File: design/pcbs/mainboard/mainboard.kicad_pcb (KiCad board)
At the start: 4 copper layers, 150 x 130 mm, 253 parts, among them J1 Conn_01x01, J10 AudioJackSw, J2 Conn_01x01, J3 Conn_01x01, J4 Conn_01x01, J5 Conn_01x04, J6 Conn_01x04, J7 Conn_Coaxial, J8 Conn_Coaxial, J9 Conn_01x03, K1 EC2-5NU, K2 EC2-5NU, K3 EC2-12NU, K4 EC2-12NU, Q1 SS8050, Q10 SS8550, Q11 SS8050, Q12 SS8050, Q2 SS8050, Q3 SS8550, Q4 SS8050, Q5 SS8050, Q6 SS8050, Q7 SS8050, Q8 SS8050, Q9 SS8050, U1 STM8S003F3P, U10 TPS79318-EP, U11 SRC4392, U12 PCM1792A, U13 OPA1612AxD, U14 Si8645BA-B-IU, U15 OPA1612AxD, U16 TPS7A30, U17 LME49600, U18 OPA1612AxD, U19 TPS7A49, U2 TPS7A49, U20 LME49600, U3 TPS7A30, U4 TLV1117-33, U5 TPS7A49, U6 KC3225K24.5760C1GE00, U7 Combo384, U8 5PB1102, U9 OPA1612AxD

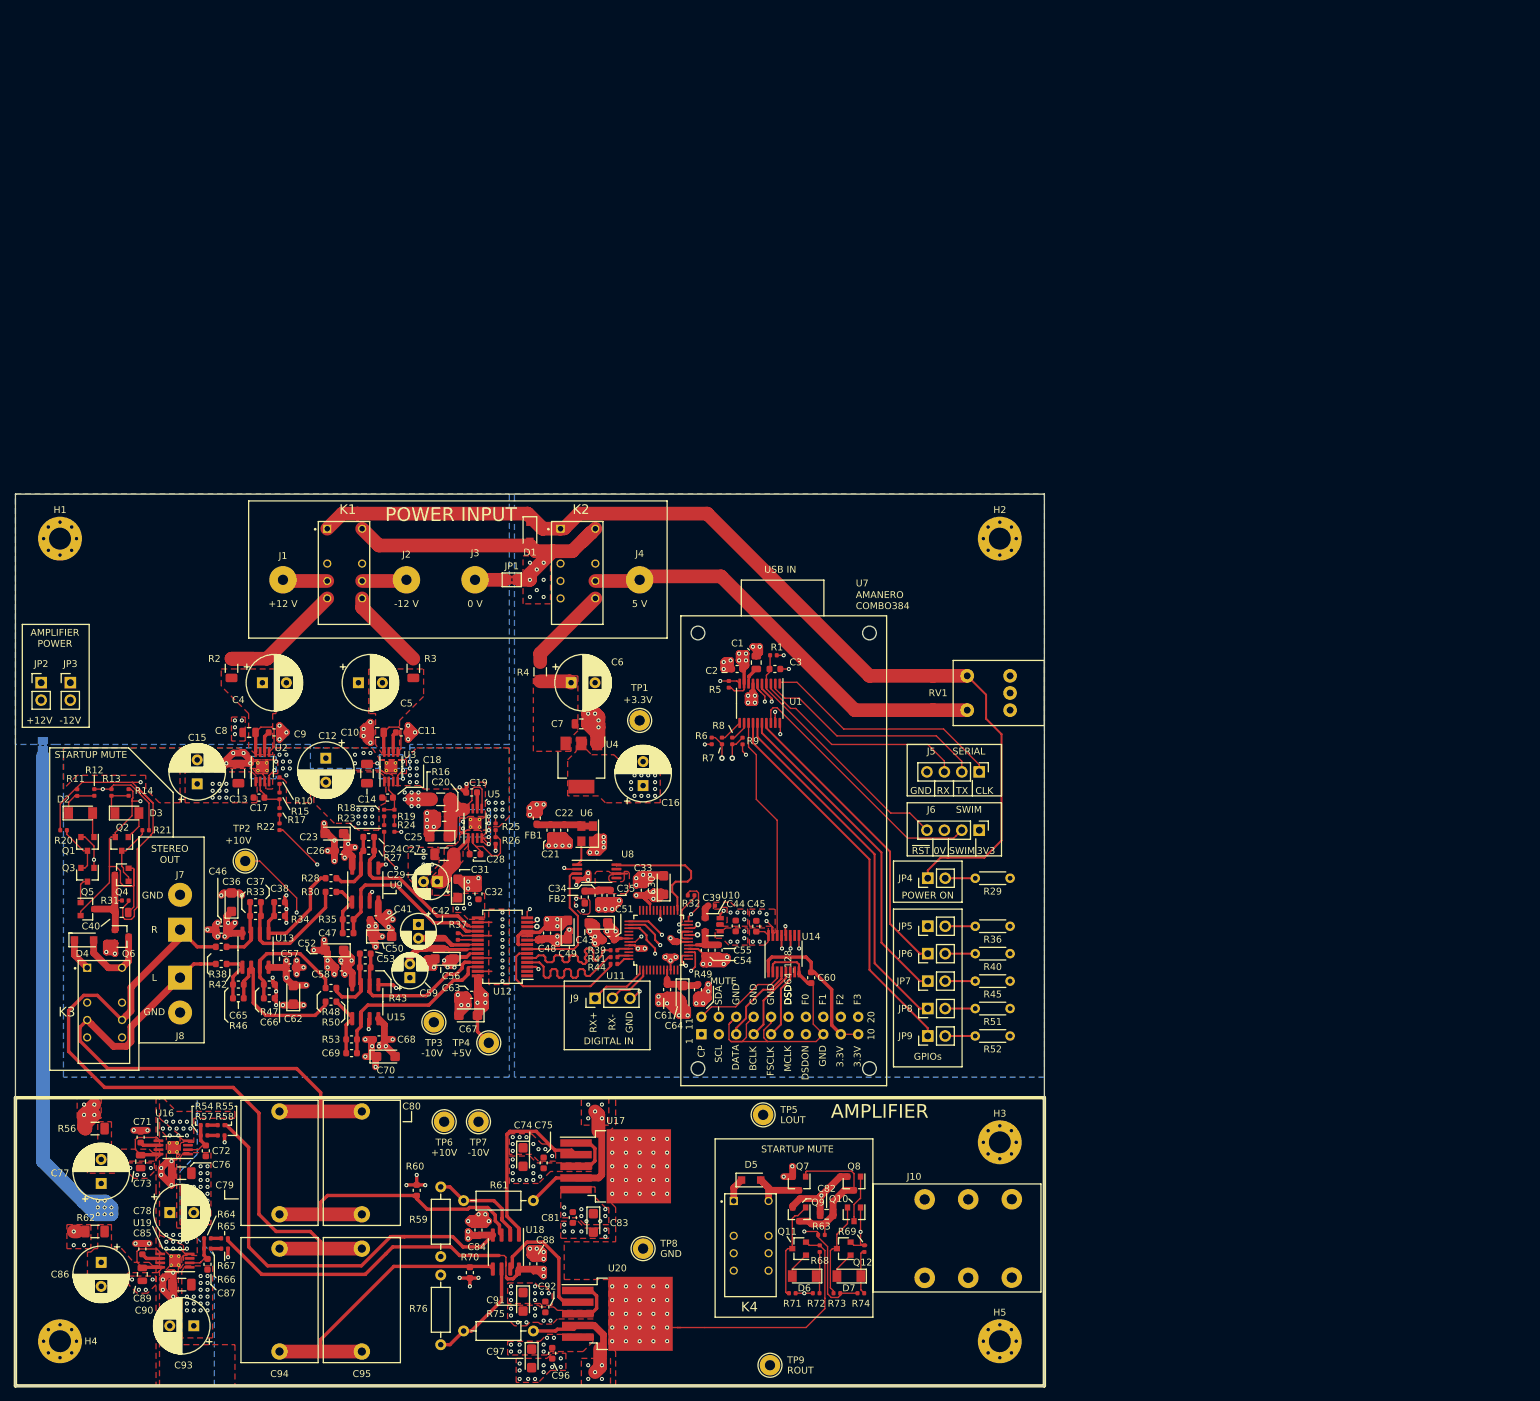
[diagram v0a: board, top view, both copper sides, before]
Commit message: Updated PCB sheet info. Clarified licence in readme.
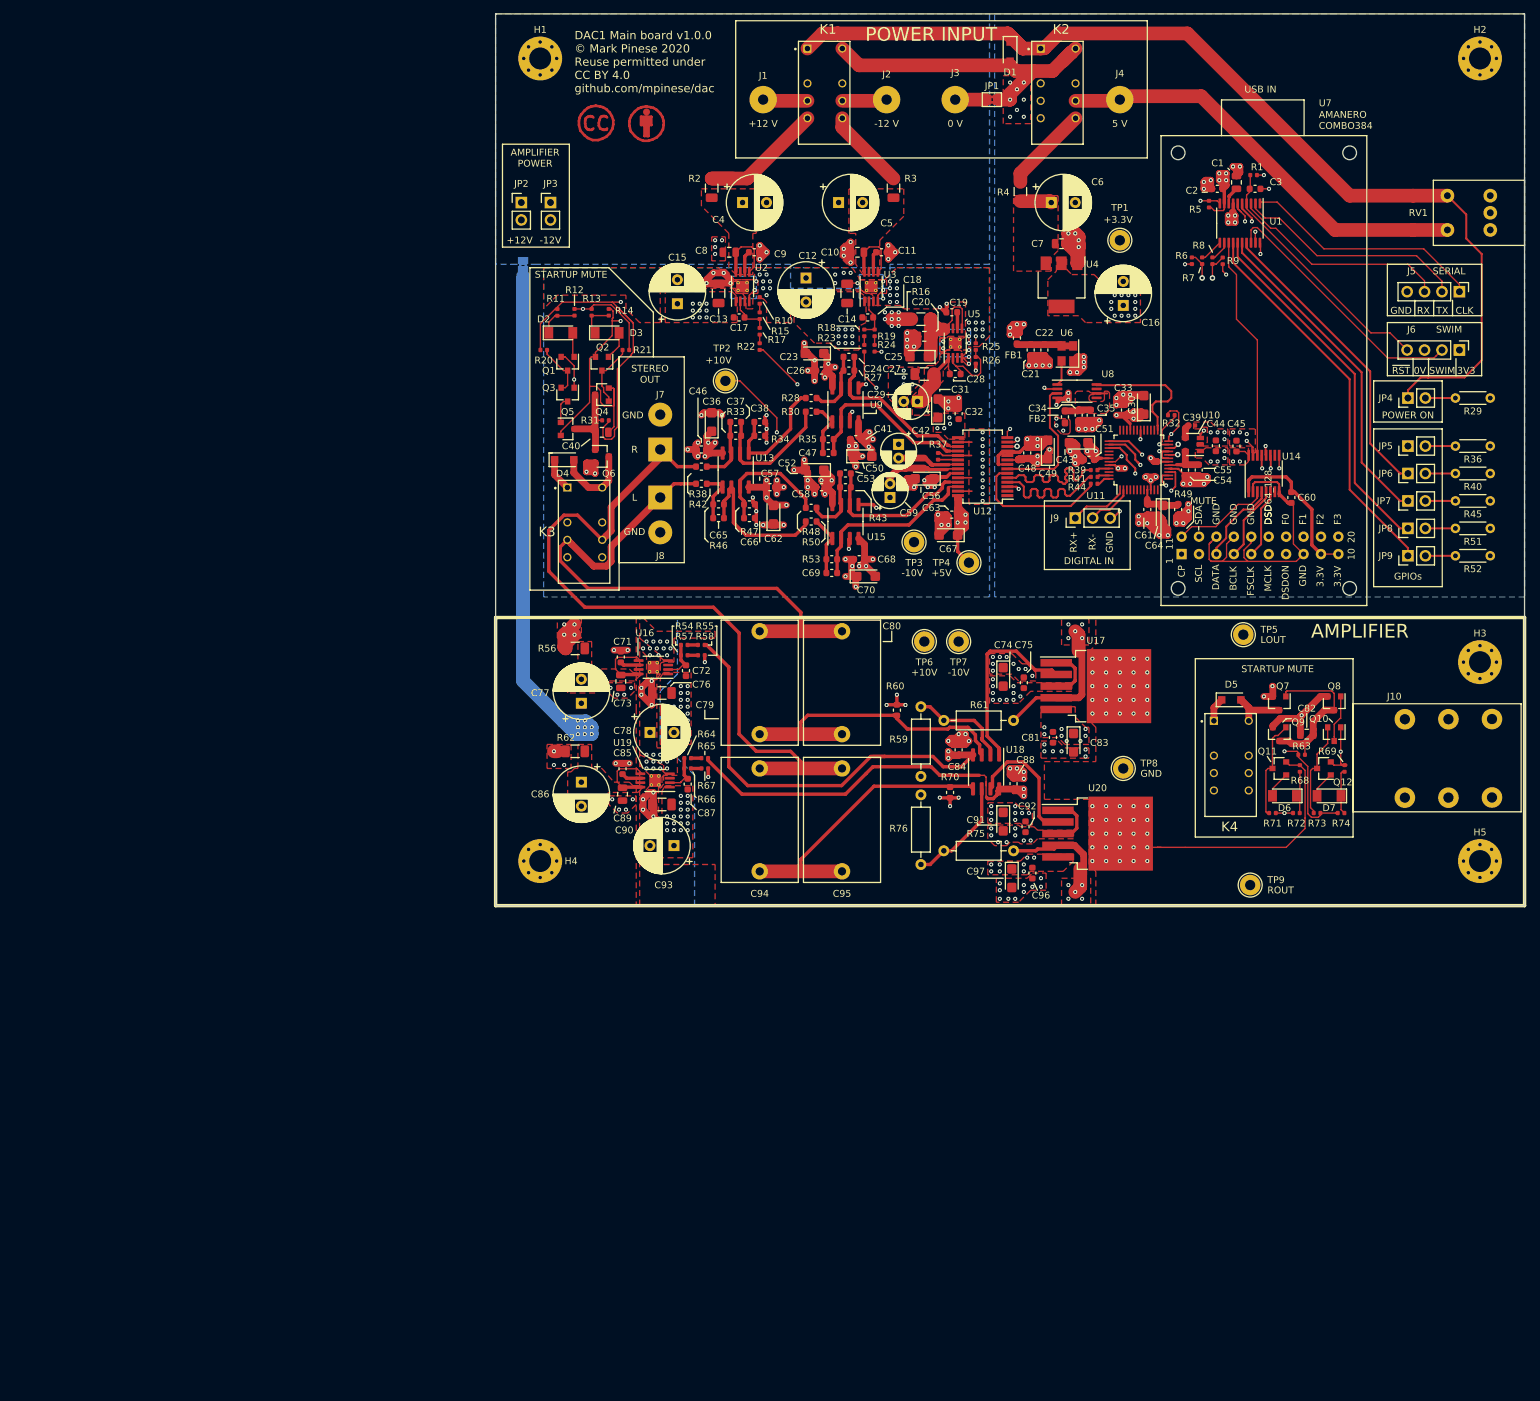
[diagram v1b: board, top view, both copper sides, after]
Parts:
- added REF**: Symbol_CC-Attribution_CopperTop_Small, Symbol:Symbol_CC-Attribution_CopperTop_Small, F.Cu at (82.0, 46.0)
- added REF**: Symbol_CreativeCommons_CopperTop_Type2_Small, Symbol:Symbol_CreativeCommons_CopperTop_Type2_Small, F.Cu at (74.5, 46.0)
- moved U10 99.0 mm to (161.6, 92.8)
- moved R6 99.0 mm to (161.5, 66.0)
- moved R7 99.0 mm to (163.0, 66.0)
- moved R72 99.0 mm to (176.7, 146.5)
- moved R8 99.0 mm to (164.5, 66.0)
- moved C1 99.0 mm to (168.0, 54.6)
- moved C10 99.0 mm to (112.8, 64.8)
- moved C11 99.0 mm to (116.2, 64.8)
- moved C12 99.0 mm to (105.2, 68.5)
- moved C13 99.0 mm to (92.5, 70.8)
- moved C14 99.0 mm to (111.2, 70.8)
- moved C15 99.0 mm to (86.5, 72.2)
- moved C16 99.0 mm to (151.5, 72.5)
- moved C17 99.0 mm to (95.5, 74.2)
- moved C18 99.0 mm to (114.2, 74.2)
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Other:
- board text added: "DAC1 Main board v1.0.0 © Mark Pinese 2020 Reuse permitted under CC BY 4.0 github.com/mpinese/dac"

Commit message: Misc updates
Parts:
- removed REF**: Symbol_CC-Attribution_CopperTop_Small, Symbol:Symbol_CC-Attribution_CopperTop_Small
- removed REF**: Symbol_CreativeCommons_CopperTop_Type2_Small, Symbol:Symbol_CreativeCommons_CopperTop_Type2_Small
- added FB3: Ferrite_Bead_Small, Resistor_SMD:R_0603_1608Metric_Pad1.05x0.95mm_HandSolder, F.Cu at (231.1, 72.5)
- C42, C59: footprint Capacitor_THT:CP_Radial_D5.0mm_P2.00mm -> Capacitor_THT:CP_Radial_D6.3mm_P2.50mm
- R29, R36, R40, R45, R51, R52: value ~ -> Optional
- R39, R41, R44: value 50 -> 10
- R6, R9: value 2.7k -> 2.4k
- moved TP3 113.4 mm to (231.0, 134.8)
- moved TP4 95.0 mm to (224.0, 113.0)
- moved C29 4.37 mm to (119.2, 82.8), turned to 270 degrees
- moved C31 4.01 mm to (128.5, 87.2), turned to 0 degrees
- moved FB1 3.25 mm to (139.0, 76.0), turned to 180 degrees
- moved C67 2.80 mm to (128.5, 104.8), turned to 0 degrees
- moved C56 2.46 mm to (124.8, 98.8), turned to 270 degrees
- moved C59 2.30 mm to (119.8, 101.0)
- moved C27 1.86 mm to (124.0, 83.6), turned to 90 degrees
- moved C42 1.60 mm to (119.8, 91.5)
- moved C63 1.35 mm to (127.8, 102.5), turned to 180 degrees
- moved C32 1.24 mm to (127.8, 89.5), turned to 180 degrees
- moved R37 0.71 mm to (125.0, 95.0), turned to 0 degrees
- moved R44 0.50 mm to (147.2, 99.0)
- moved R41 0.25 mm to (147.2, 97.8)
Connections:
- C21 pad 1: GNDD -> GND
- C22 pad 1: GNDD -> GND
- C34 pad 1: GNDD -> GND
- C35 pad 1: GNDD -> GND
- C48 pad 2: GNDD -> GND
- C49 pad 2: GNDD -> GND
- U12 pad 8: GNDD -> GND
- U12 pad 9: +3V3 -> Net-(FB3-Pad2)
- U6 pad 1: GNDD -> GND
- U8 pad 4: GNDD -> GND
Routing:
- net /DAC/+5V: track 129.3 -> 8.48 mm, vias 11 -> 10
- net GNDD: track 233.8 -> 163.3 mm, vias 75 -> 56
- net GND: track 214.1 -> 171.3 mm, vias 133 -> 106
- net +3V3: track 101.1 -> 70.0 mm, vias 50 -> 37
- net /ASRC/I2C_SDA: track 57.7 -> 31.2 mm, vias 3 -> 2
- net /ASRC/MCLK: track 19.5 -> 0.00 mm
- net /DAC/MCLK: track 19.4 -> 0.00 mm
- net /ASRC/I2C_SCL: track 62.0 -> 47.9 mm, vias 3 -> 2
- net Net-(C59-Pad2): track 21.3 -> 8.55 mm
- net -10V: track 239.5 -> 228.6 mm
- net Net-(C21-Pad2): track 8.31 -> 0.00 mm
- net /DAC/SDIN: track 20.8 -> 12.6 mm
- net /DAC/LRCKIN: track 20.5 -> 12.4 mm
- net Net-(C42-Pad2): track 14.7 -> 8.34 mm
- net Net-(C34-Pad2): track 5.38 -> 0.00 mm
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- removed copper zone on F.Cu, net Net-(C34-Pad2)
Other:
- board text added: "Stackup: JLC7628 1.6 mm Stackup over digital: SIG GNDD SIG 3.3V Stackup over analog SIG UNUSED +5, +/-10 rails GND Enclosure: Hammond 1455P or 1455R"
- board text removed: "Stackup: JLC7628 1.6 mm Stackup over digital: SIG GNDD SIG 3.3V Stackup over analog SIG UNUSED +5, +/-10 rails GND"
